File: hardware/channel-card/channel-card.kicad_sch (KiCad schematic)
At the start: 0 parts

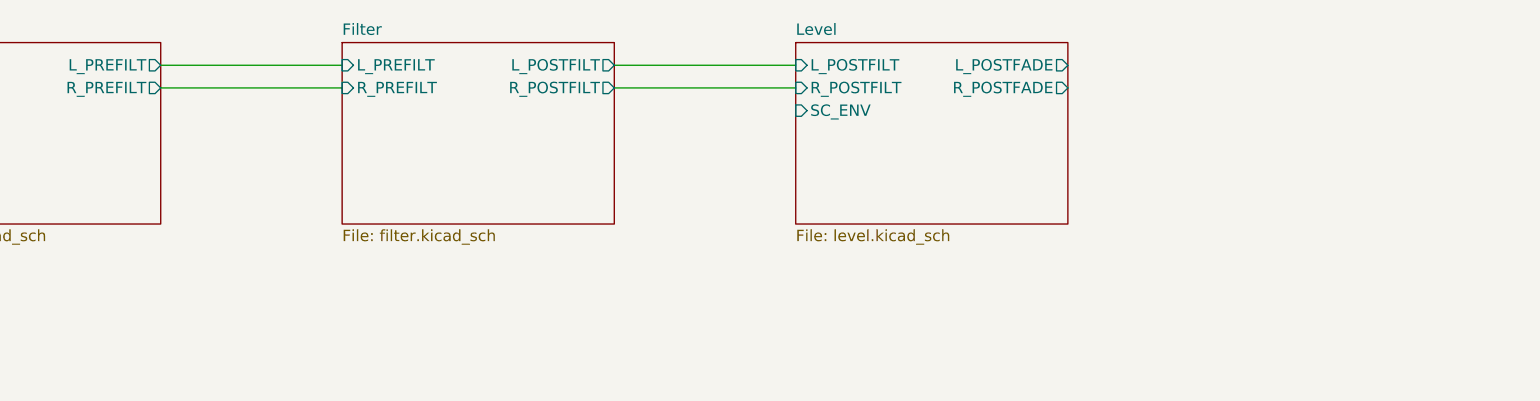
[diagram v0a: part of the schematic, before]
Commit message: Add channel card routing sheet
Pre-fader buffers, two stereo AUX sends with dual-gang pots and pre/post
jumpers, DG413 main/compressor bus assign, DG412 PFL and sidechain send,
open-collector PFL_ACT driver and three buttons, drawn with real wires
and checked against routing_build.py. Bus resistors 22.1k (decision 74).
root_links.py labels shared sheet pins on the root sheet.

Co-Authored-By: Claude Opus 5.5 <noreply@anthropic.com>
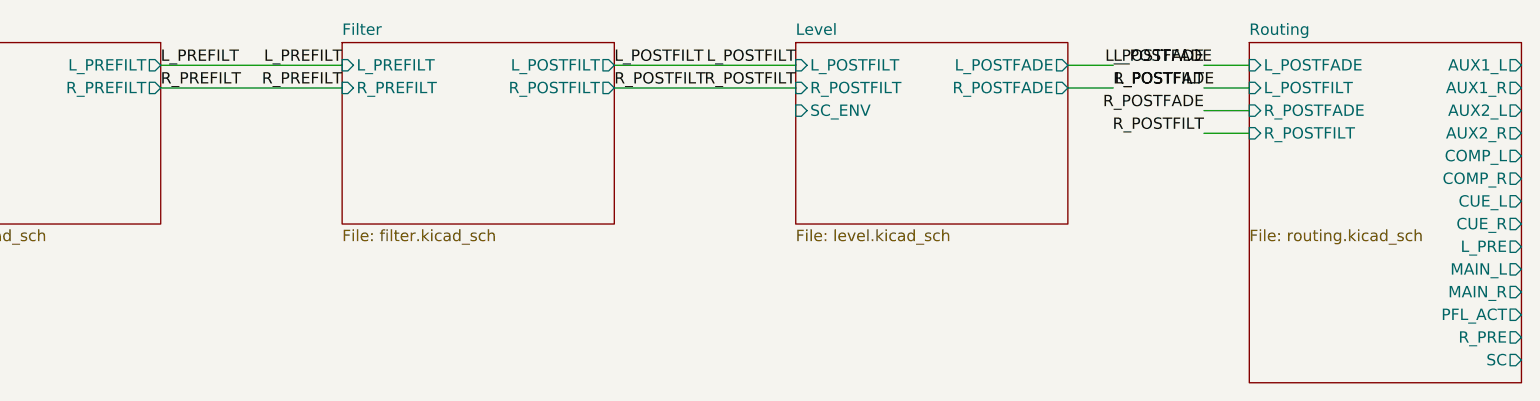
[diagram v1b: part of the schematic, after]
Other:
- added sheet Routing (routing.kicad_sch)

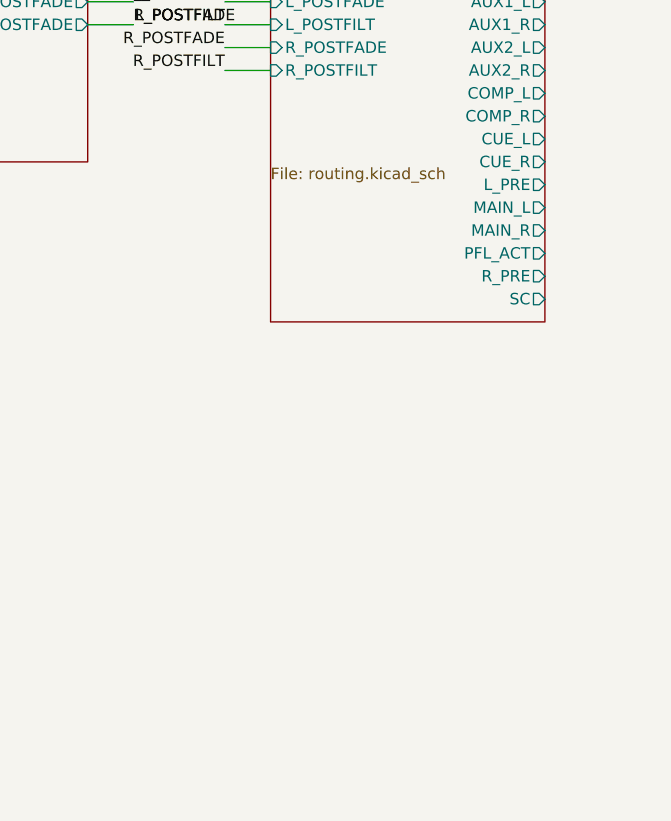
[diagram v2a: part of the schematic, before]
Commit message: Add channel card meter sheet
8-segment peak meter on the pre-fader signal: four superdiode peak
detectors into one hold capacitor (1 ms attack, about 1.5 s fall),
buffered into eight LM339 comparators against a 1% ladder from +15 V,
LEDs from +5 V (decision 76). Drawn with real wires and checked against
meter_build.py. Page numbers now order by sheet position in both axes.
Adds a 10-segment gauge bar sample to the second Electrokit order.

Co-Authored-By: Claude Opus 5.5 <noreply@anthropic.com>
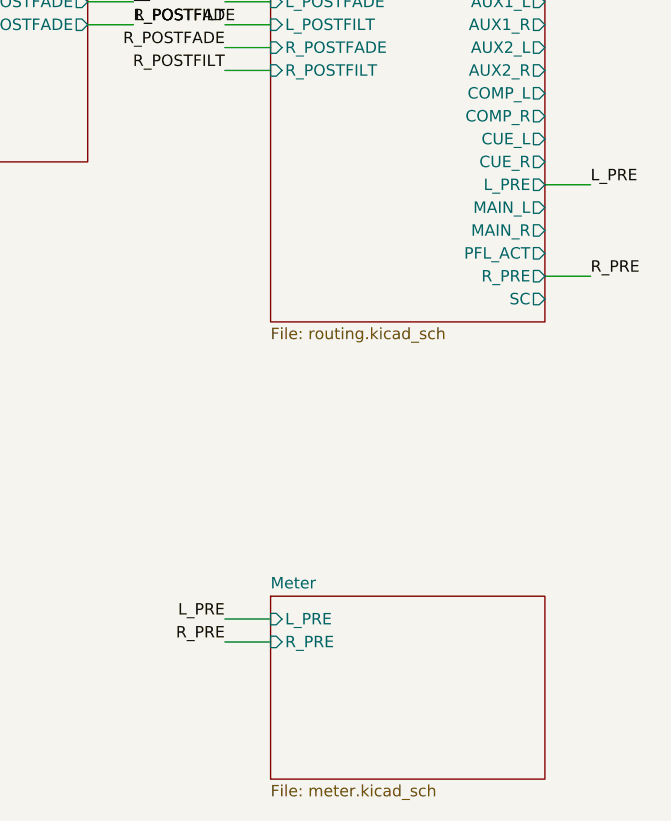
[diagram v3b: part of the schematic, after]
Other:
- added sheet Meter (meter.kicad_sch)
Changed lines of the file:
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@@
 		)
 		(property "Sheetfile" "routing.kicad_sch"
-			(at 177.8 59.0046 0)
+			(at 177.8 76.7846 0)
 			(effects
 				(font
@@
 		)
 		(pin "AUX1_L" output
-			(at 208.28 40.64 0)
+			(at 208.28 40.64 0.0000)
 			(effects
 				(font
@@
 		)
 		(pin "AUX1_R" output
-			(at 208.28 43.18 0)
+			(at 208.28 43.18 0.0000)
 			(effects
 				(font
@@
 		)
 		(pin "AUX2_L" output
-			(at 208.28 45.72 0)
+			(at 208.28 45.72 0.0000)
 			(effects
 				(font
@@
 		)
 		(pin "AUX2_R" output
-			(at 208.28 48.26 0)
+			(at 208.28 48.26 0.0000)
 			(effects
 				(font
@@
 		)
 		(pin "COMP_L" output
-			(at 208.28 50.8 0)
+			(at 208.28 50.8 0.0000)
 			(effects
 				(font
@@
 		)
 		(pin "COMP_R" output
-			(at 208.28 53.34 0)
+			(at 208.28 53.34 0.0000)
 			(effects
 				(font
@@
 		)
 		(pin "CUE_L" output
-			(at 208.28 55.88 0)
+			(at 208.28 55.88 0.0000)
 			(effects
 				(font
@@
 		)
 		(pin "CUE_R" output
-			(at 208.28 58.42 0)
+			(at 208.28 58.42 0.0000)
 			(effects
 				(font
@@
 		)
 		(pin "L_PRE" output
-			(at 208.28 60.96 0)
+			(at 208.28 60.96 0.0000)
 			(effects
 				(font
@@
 		)
 		(pin "MAIN_L" output
-			(at 208.28 63.5 0)
+			(at 208.28 63.5 0.0000)
 			(effects
 				(font
@@
 		)
 		(pin "MAIN_R" output
-			(at 208.28 66.04 0)
+			(at 208.28 66.04 0.0000)
 			(effects
 				(font
@@
 		)
 		(pin "PFL_ACT" output
-			(at 208.28 68.58 0)
+			(at 208.28 68.58 0.0000)
 			(effects
 				(font
@@
 		)
 		(pin "R_PRE" output
-			(at 208.28 71.12 0)
+			(at 208.28 71.12 0.0000)
 			(effects
 				(font
@@
 		)
 		(pin "SC" output
-			(at 208.28 73.66 0)
+			(at 208.28 73.66 0.0000)
 			(effects
 				(font
@@
 				(path "/44b8098e-8b91-4d90-8e36-746977844050"
 					(page "5")
+				)
+			)
+		)
+	)
+	(sheet
+		(at 177.8 106.68)
+		(size 30.48 20.32)
+		(exclude_from_sim no)
+		(in_bom yes)
+		(on_board yes)
+		(dnp no)
+		(fields_autoplaced yes)
+		(stroke
+			(width 0.1524)
+			(type solid)
+		)
+		(fill
+			(color 0 0 0 0.0000)
+		)
+		(property "Sheetname" "Meter"
+			(at 177.8 105.9684 0)
+			(effects
+				(font
+					(size 1.27 1.27)
+				)
+				(justify left bottom)
+			)
+		)
+		(property "Sheetfile" "meter.kicad_sch"
+			(at 177.8 127.5846 0)
+			(effects
+				(font
+					(size 1.27 1.27)
+				)
+				(justify left top)
+			)
+		)
+		(pin "L_PRE" input
+			(at 177.8 109.22 180)
+			(effects
+				(font
+					(size 1.27 1.27)
+				)
+				(justify left)
+			)
+		)
+		(pin "R_PRE" input
+			(at 177.8 111.76 180)
+			(effects
+				(font
+					(size 1.27 1.27)
+				)
+				(justify left)
+			)
+		)
+		(instances
+			(project "channel-card"
+				(path "/44b8098e-8b91-4d90-8e36-746977844050"
+					(page "6")
 				)
 			)
@@
 	(wire (pts (xy 177.8 48.26) (xy 172.72 48.26)) (stroke (width 0) (type default)))
 	(label "R_POSTFILT" (at 172.72 48.26 180) (fields_autoplaced yes) (effects (font (size 1.27 1.27)) (justify right bottom)))
+	(wire (pts (xy 208.28 60.96) (xy 213.36 60.96)) (stroke (width 0) (type default)))
+	(label "L_PRE" (at 213.36 60.96 0) (fields_autoplaced yes) (effects (font (size 1.27 1.27)) (justify left bottom)))
+	(wire (pts (xy 208.28 71.12) (xy 213.36 71.12)) (stroke (width 0) (type default)))
+	(label "R_PRE" (at 213.36 71.12 0) (fields_autoplaced yes) (effects (font (size 1.27 1.27)) (justify left bottom)))
+	(wire (pts (xy 177.8 109.22) (xy 172.72 109.22)) (stroke (width 0) (type default)))
+	(label "L_PRE" (at 172.72 109.22 180) (fields_autoplaced yes) (effects (font (size 1.27 1.27)) (justify right bottom)))
+	(wire (pts (xy 177.8 111.76) (xy 172.72 111.76)) (stroke (width 0) (type default)))
+	(label "R_PRE" (at 172.72 111.76 180) (fields_autoplaced yes) (effects (font (size 1.27 1.27)) (justify right bottom)))
 	(sheet_instances
 		(path "/"

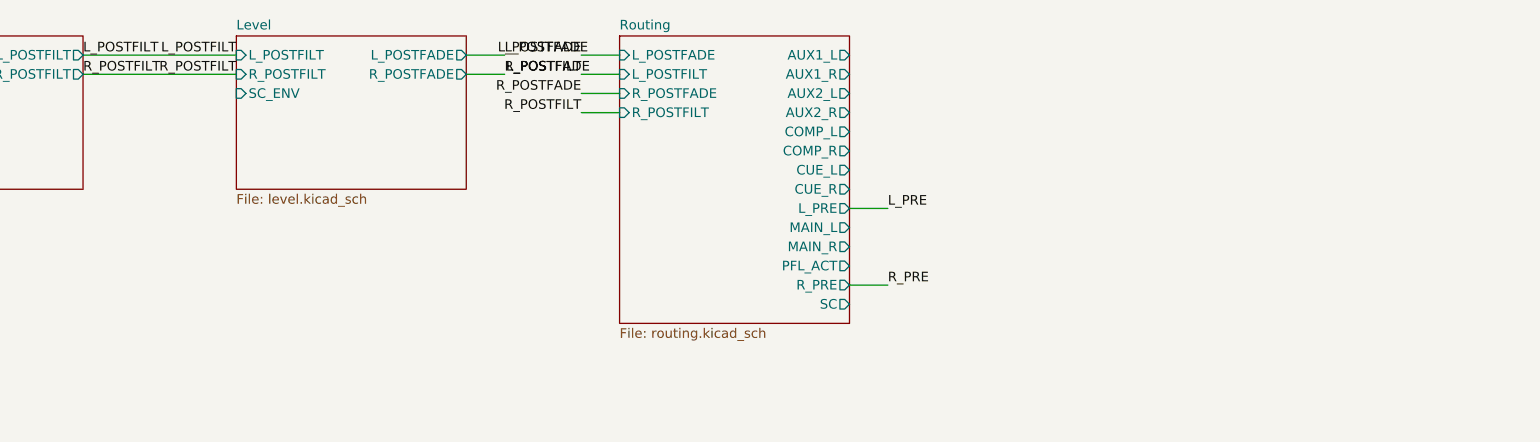
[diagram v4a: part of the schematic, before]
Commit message: Add chain and power sheet; channel card schematic complete
Audio and power ribbon IN/OUT headers wired straight through,
LM317/LM337 regulators to +/-15.2 V with ADJ bypass and protection
diodes, SS14 rail clamps, 78L05 for +5 V, and test pads for the rails
(decision 78). Power flags moved to this sheet. The whole channel card
now passes ERC with 0 errors and 0 warnings and every sheet matches its
reference netlist. Records the open power-ribbon current question in
CHAIN.md.

Co-Authored-By: Claude Opus 5.5 <noreply@anthropic.com>
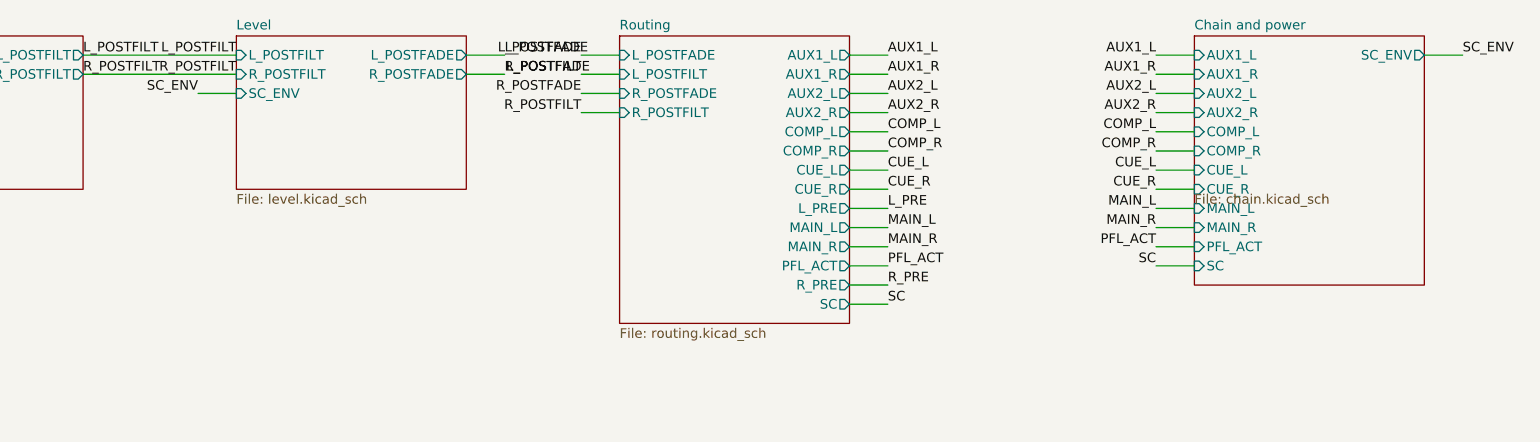
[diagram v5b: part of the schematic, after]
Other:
- added sheet Chain and power (chain.kicad_sch)
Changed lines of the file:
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@@
+		)
+	)
+	(sheet
+		(at 254 38.1)
+		(size 30.48 33.02)
+		(exclude_from_sim no)
+		(in_bom yes)
+		(on_board yes)
+		(dnp no)
+		(fields_autoplaced yes)
+		(stroke
+			(width 0.1524)
+			(type solid)
+		)
+		(fill
+			(color 0 0 0 0.0000)
+		)
+		(property "Sheetname" "Chain and power"
+			(at 254 37.3884 0)
+			(effects
+				(font
+					(size 1.27 1.27)
+				)
+				(justify left bottom)
+			)
+		)
+		(property "Sheetfile" "chain.kicad_sch"
+			(at 254 59.0046 0)
+			(effects
+				(font
+					(size 1.27 1.27)
+				)
+				(justify left top)
+			)
+		)
+		(pin "AUX1_L" input
+			(at 254 40.64 180)
+			(effects
+				(font
+					(size 1.27 1.27)
+				)
+				(justify left)
+			)
+		)
+		(pin "AUX1_R" input
+			(at 254 43.18 180)
+			(effects
+				(font
+					(size 1.27 1.27)
+				)
+				(justify left)
+			)
+		)
+		(pin "AUX2_L" input
+			(at 254 45.72 180)
+			(effects
+				(font
+					(size 1.27 1.27)
+				)
+				(justify left)
+			)
+		)
+		(pin "AUX2_R" input
+			(at 254 48.26 180)
+			(effects
+				(font
+					(size 1.27 1.27)
+				)
+				(justify left)
+			)
+		)
+		(pin "COMP_L" input
+			(at 254 50.8 180)
+			(effects
+				(font
+					(size 1.27 1.27)
+				)
+				(justify left)
+			)
+		)
+		(pin "COMP_R" input
+			(at 254 53.34 180)
+			(effects
+				(font
+					(size 1.27 1.27)
+				)
+				(justify left)
+			)
+		)
+		(pin "CUE_L" input
+			(at 254 55.88 180)
+			(effects
+				(font
+					(size 1.27 1.27)
+				)
+				(justify left)
+			)
+		)
+		(pin "CUE_R" input
+			(at 254 58.42 180)
+			(effects
+				(font
+					(size 1.27 1.27)
+				)
+				(justify left)
+			)
+		)
+		(pin "MAIN_L" input
+			(at 254 60.96 180)
+			(effects
+				(font
+					(size 1.27 1.27)
+				)
+				(justify left)
+			)
+		)
+		(pin "MAIN_R" input
+			(at 254 63.5 180)
+			(effects
+				(font
+					(size 1.27 1.27)
+				)
+				(justify left)
+			)
+		)
+		(pin "PFL_ACT" input
+			(at 254 66.04 180)
+			(effects
+				(font
+					(size 1.27 1.27)
+				)
+				(justify left)
+			)
+		)
+		(pin "SC" input
+			(at 254 68.58 180)
+			(effects
+				(font
+					(size 1.27 1.27)
+				)
+				(justify left)
+			)
+		)
+		(pin "SC_ENV" output
+			(at 284.48 40.64 0)
+			(effects
+				(font
+					(size 1.27 1.27)
+				)
+				(justify right)
+			)
+		)
+		(instances
+			(project "channel-card"
+				(path "/44b8098e-8b91-4d90-8e36-746977844050"
+					(page "7")
+				)
+			)
 		)
 	)
@@
 	(label "L_POSTFILT" (at 127 40.64 180) (fields_autoplaced yes) (effects (font (size 1.27 1.27)) (justify right bottom)))
 	(label "R_POSTFILT" (at 127 43.18 180) (fields_autoplaced yes) (effects (font (size 1.27 1.27)) (justify right bottom)))
+	(wire (pts (xy 127 45.72) (xy 121.92 45.72)) (stroke (width 0) (type default)))
+	(label "SC_ENV" (at 121.92 45.72 180) (fields_autoplaced yes) (effects (font (size 1.27 1.27)) (justify right bottom)))
 	(wire (pts (xy 157.48 40.64) (xy 162.56 40.64)) (stroke (width 0) (type default)))
 	(label "L_POSTFADE" (at 162.56 40.64 0) (fields_autoplaced yes) (effects (font (size 1.27 1.27)) (justify left bottom)))
@@
 	(wire (pts (xy 177.8 48.26) (xy 172.72 48.26)) (stroke (width 0) (type default)))
 	(label "R_POSTFILT" (at 172.72 48.26 180) (fields_autoplaced yes) (effects (font (size 1.27 1.27)) (justify right bottom)))
+	(wire (pts (xy 208.28 40.64) (xy 213.36 40.64)) (stroke (width 0) (type default)))
+	(label "AUX1_L" (at 213.36 40.64 0) (fields_autoplaced yes) (effects (font (size 1.27 1.27)) (justify left bottom)))
+	(wire (pts (xy 208.28 43.18) (xy 213.36 43.18)) (stroke (width 0) (type default)))
+	(label "AUX1_R" (at 213.36 43.18 0) (fields_autoplaced yes) (effects (font (size 1.27 1.27)) (justify left bottom)))
+	(wire (pts (xy 208.28 45.72) (xy 213.36 45.72)) (stroke (width 0) (type default)))
+	(label "AUX2_L" (at 213.36 45.72 0) (fields_autoplaced yes) (effects (font (size 1.27 1.27)) (justify left bottom)))
+	(wire (pts (xy 208.28 48.26) (xy 213.36 48.26)) (stroke (width 0) (type default)))
+	(label "AUX2_R" (at 213.36 48.26 0) (fields_autoplaced yes) (effects (font (size 1.27 1.27)) (justify left bottom)))
+	(wire (pts (xy 208.28 50.8) (xy 213.36 50.8)) (stroke (width 0) (type default)))
+	(label "COMP_L" (at 213.36 50.8 0) (fields_autoplaced yes) (effects (font (size 1.27 1.27)) (justify left bottom)))
+	(wire (pts (xy 208.28 53.34) (xy 213.36 53.34)) (stroke (width 0) (type default)))
+	(label "COMP_R" (at 213.36 53.34 0) (fields_autoplaced yes) (effects (font (size 1.27 1.27)) (justify left bottom)))
+	(wire (pts (xy 208.28 55.88) (xy 213.36 55.88)) (stroke (width 0) (type default)))
+	(label "CUE_L" (at 213.36 55.88 0) (fields_autoplaced yes) (effects (font (size 1.27 1.27)) (justify left bottom)))
+	(wire (pts (xy 208.28 58.42) (xy 213.36 58.42)) (stroke (width 0) (type default)))
+	(label "CUE_R" (at 213.36 58.42 0) (fields_autoplaced yes) (effects (font (size 1.27 1.27)) (justify left bottom)))
 	(wire (pts (xy 208.28 60.96) (xy 213.36 60.96)) (stroke (width 0) (type default)))
 	(label "L_PRE" (at 213.36 60.96 0) (fields_autoplaced yes) (effects (font (size 1.27 1.27)) (justify left bottom)))
+	(wire (pts (xy 208.28 63.5) (xy 213.36 63.5)) (stroke (width 0) (type default)))
+	(label "MAIN_L" (at 213.36 63.5 0) (fields_autoplaced yes) (effects (font (size 1.27 1.27)) (justify left bottom)))
+	(wire (pts (xy 208.28 66.04) (xy 213.36 66.04)) (stroke (width 0) (type default)))
+	(label "MAIN_R" (at 213.36 66.04 0) (fields_autoplaced yes) (effects (font (size 1.27 1.27)) (justify left bottom)))
+	(wire (pts (xy 208.28 68.58) (xy 213.36 68.58)) (stroke (width 0) (type default)))
+	(label "PFL_ACT" (at 213.36 68.58 0) (fields_autoplaced yes) (effects (font (size 1.27 1.27)) (justify left bottom)))
 	(wire (pts (xy 208.28 71.12) (xy 213.36 71.12)) (stroke (width 0) (type default)))
 	(label "R_PRE" (at 213.36 71.12 0) (fields_autoplaced yes) (effects (font (size 1.27 1.27)) (justify left bottom)))
+	(wire (pts (xy 208.28 73.66) (xy 213.36 73.66)) (stroke (width 0) (type default)))
+	(label "SC" (at 213.36 73.66 0) (fields_autoplaced yes) (effects (font (size 1.27 1.27)) (justify left bottom)))
 	(wire (pts (xy 177.8 109.22) (xy 172.72 109.22)) (stroke (width 0) (type default)))
 	(label "L_PRE" (at 172.72 109.22 180) (fields_autoplaced yes) (effects (font (size 1.27 1.27)) (justify right bottom)))
 	(wire (pts (xy 177.8 111.76) (xy 172.72 111.76)) (stroke (width 0) (type default)))
 	(label "R_PRE" (at 172.72 111.76 180) (fields_autoplaced yes) (effects (font (size 1.27 1.27)) (justify right bottom)))
+	(wire (pts (xy 254 40.64) (xy 248.92 40.64)) (stroke (width 0) (type default)))
+	(label "AUX1_L" (at 248.92 40.64 180) (fields_autoplaced yes) (effects (font (size 1.27 1.27)) (justify right bottom)))
+	(wire (pts (xy 254 43.18) (xy 248.92 43.18)) (stroke (width 0) (type default)))
+	(label "AUX1_R" (at 248.92 43.18 180) (fields_autoplaced yes) (effects (font (size 1.27 1.27)) (justify right bottom)))
+	(wire (pts (xy 254 45.72) (xy 248.92 45.72)) (stroke (width 0) (type default)))
+	(label "AUX2_L" (at 248.92 45.72 180) (fields_autoplaced yes) (effects (font (size 1.27 1.27)) (justify right bottom)))
+	(wire (pts (xy 254 48.26) (xy 248.92 48.26)) (stroke (width 0) (type default)))
+	(label "AUX2_R" (at 248.92 48.26 180) (fields_autoplaced yes) (effects (font (size 1.27 1.27)) (justify right bottom)))
+	(wire (pts (xy 254 50.8) (xy 248.92 50.8)) (stroke (width 0) (type default)))
+	(label "COMP_L" (at 248.92 50.8 180) (fields_autoplaced yes) (effects (font (size 1.27 1.27)) (justify right bottom)))
+	(wire (pts (xy 254 53.34) (xy 248.92 53.34)) (stroke (width 0) (type default)))
+	(label "COMP_R" (at 248.92 53.34 180) (fields_autoplaced yes) (effects (font (size 1.27 1.27)) (justify right bottom)))
+	(wire (pts (xy 254 55.88) (xy 248.92 55.88)) (stroke (width 0) (type default)))
+	(label "CUE_L" (at 248.92 55.88 180) (fields_autoplaced yes) (effects (font (size 1.27 1.27)) (justify right bottom)))
+	(wire (pts (xy 254 58.42) (xy 248.92 58.42)) (stroke (width 0) (type default)))
+	(label "CUE_R" (at 248.92 58.42 180) (fields_autoplaced yes) (effects (font (size 1.27 1.27)) (justify right bottom)))
+	(wire (pts (xy 254 60.96) (xy 248.92 60.96)) (stroke (width 0) (type default)))
+	(label "MAIN_L" (at 248.92 60.96 180) (fields_autoplaced yes) (effects (font (size 1.27 1.27)) (justify right bottom)))
+	(wire (pts (xy 254 63.5) (xy 248.92 63.5)) (stroke (width 0) (type default)))
+	(label "MAIN_R" (at 248.92 63.5 180) (fields_autoplaced yes) (effects (font (size 1.27 1.27)) (justify right bottom)))
+	(wire (pts (xy 254 66.04) (xy 248.92 66.04)) (stroke (width 0) (type default)))
+	(label "PFL_ACT" (at 248.92 66.04 180) (fields_autoplaced yes) (effects (font (size 1.27 1.27)) (justify right bottom)))
+	(wire (pts (xy 254 68.58) (xy 248.92 68.58)) (stroke (width 0) (type default)))
+	(label "SC" (at 248.92 68.58 180) (fields_autoplaced yes) (effects (font (size 1.27 1.27)) (justify right bottom)))
+	(wire (pts (xy 284.48 40.64) (xy 289.56 40.64)) (stroke (width 0) (type default)))
+	(label "SC_ENV" (at 289.56 40.64 0) (fields_autoplaced yes) (effects (font (size 1.27 1.27)) (justify left bottom)))
 	(sheet_instances
 		(path "/"
